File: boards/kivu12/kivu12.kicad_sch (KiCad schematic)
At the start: 26 parts, among them J1 P1, J10 SD, J11 GND, J12 LX2, J2 CIX, J3 BX, J4 LX1, J5 ANALOG, J6 POWER2, J7 BX, J9 POWER1

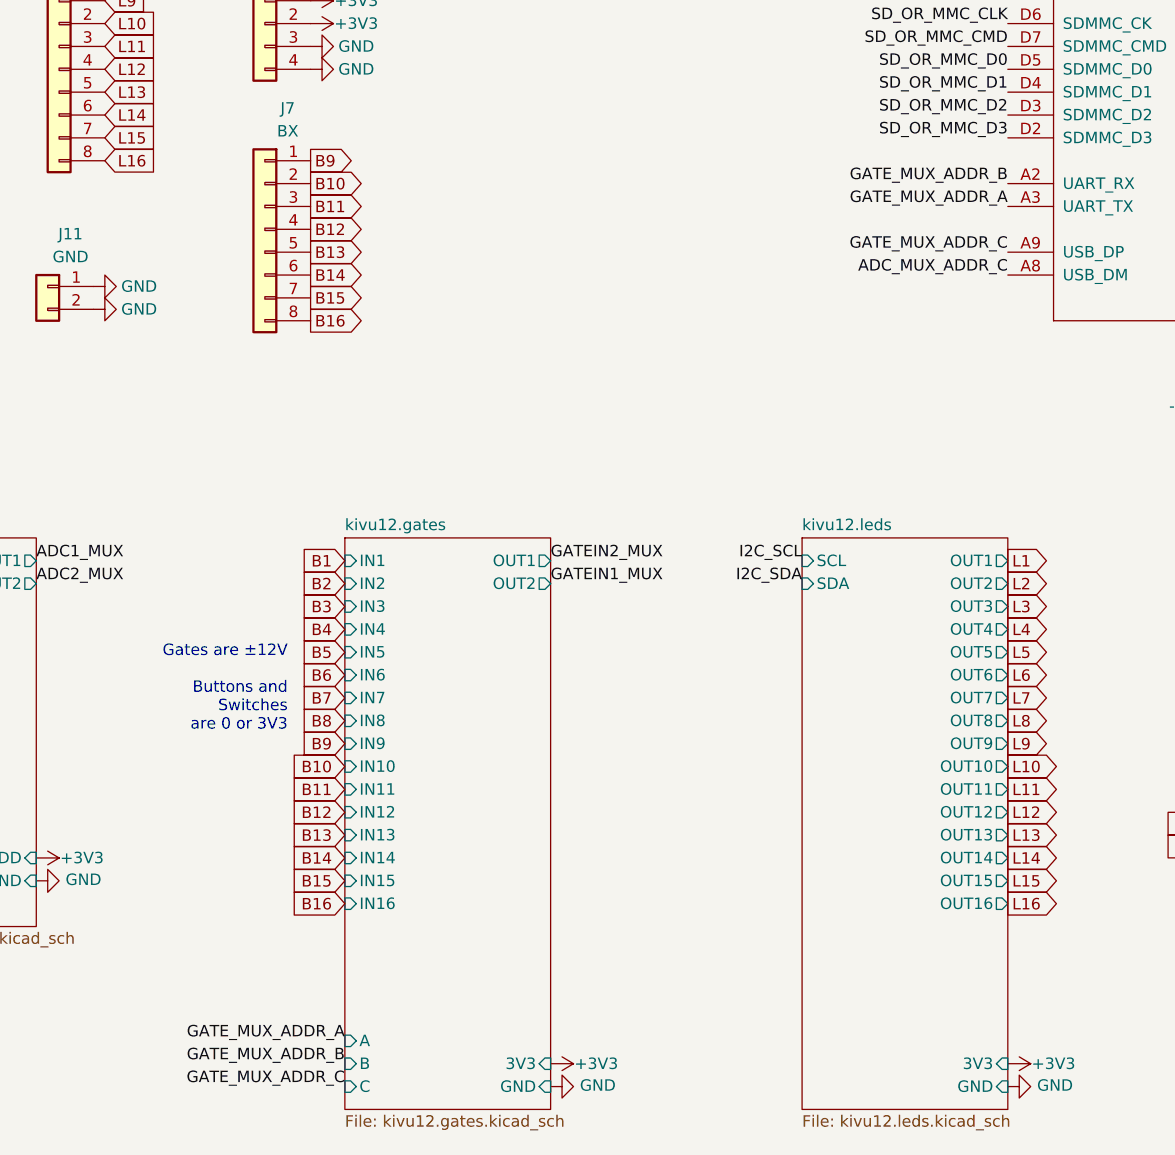
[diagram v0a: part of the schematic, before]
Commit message: Use shift register instead of multiplexer
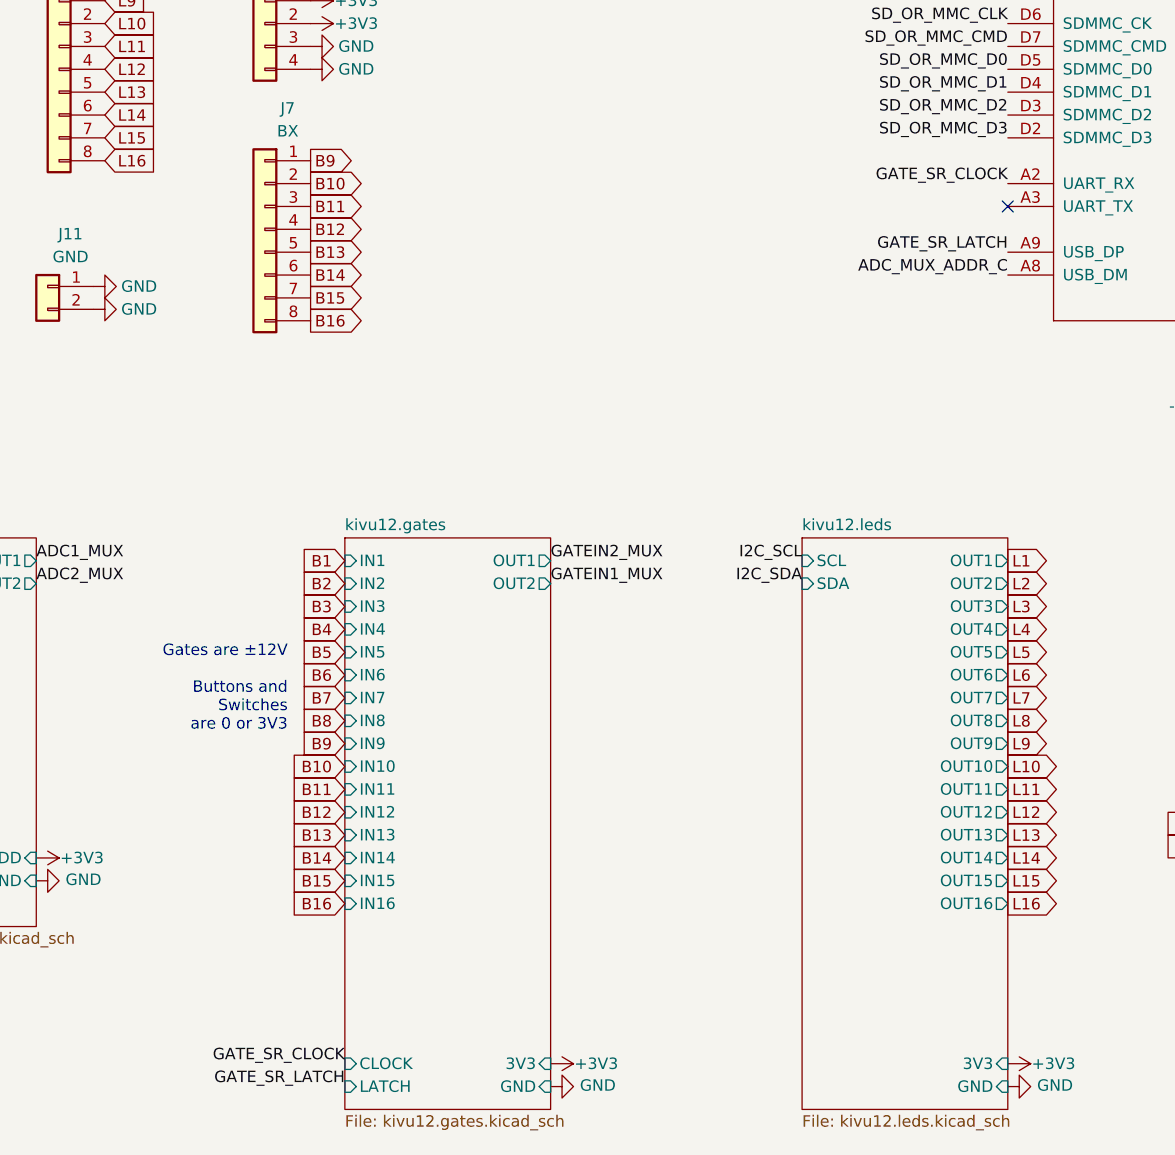
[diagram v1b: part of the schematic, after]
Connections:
- net GATE_MUX_ADDR_A: no longer names the net of DPSM1.A3 (UART_TX)
- net GATE_MUX_ADDR_B renamed GATE_SR_CLOCK
- net GATE_MUX_ADDR_C renamed GATE_SR_LATCH
- no-connect marks 1 -> 2
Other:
- sheet kivu12.gates ports: added CLOCK, LATCH; removed A, B, C
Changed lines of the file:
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@@
   (paper "A4")
   (no_connect (at 176.53 26.67))
+  (no_connect (at 158.75 77.47))
   (text "Just needed for BOM\nThey are:\n- 4x 2x5 female socket for the DPSM\n- 1x 1x36 Male header\n- 8x Jumpers"
     (at 246.38 57.15 0)
@@
     (effects (font (size 1.27 1.27)) (justify right bottom))
   )
-  (label "GATE_MUX_ADDR_C" (at 158.75 82.55 180)
+  (label "GATE_SR_LATCH" (at 158.75 82.55 180)
     (effects (font (size 1.27 1.27)) (justify right bottom))
   )
@@
     (effects (font (size 1.27 1.27)) (justify left bottom))
   )
-  (label "GATE_MUX_ADDR_B" (at 158.75 74.93 180)
+  (label "GATE_SR_CLOCK" (at 158.75 74.93 180)
     (effects (font (size 1.27 1.27)) (justify right bottom))
   )
@@
     (effects (font (size 1.27 1.27)) (justify right bottom))
   )
-  (label "GATE_MUX_ADDR_A" (at 158.75 77.47 180)
-    (effects (font (size 1.27 1.27)) (justify right bottom))
-  )
-  (label "GATE_MUX_ADDR_A" (at 85.09 170.18 180)
-    (effects (font (size 1.27 1.27)) (justify right bottom))
-  )
   (label "CV_OR_PITCH_ADSR2" (at 158.75 36.83 180)
     (effects (font (size 1.27 1.27)) (justify right bottom))
@@
     (effects (font (size 1.27 1.27)) (justify left bottom))
   )
-  (label "GATE_MUX_ADDR_C" (at 85.09 175.26 180)
+  (label "GATE_SR_LATCH" (at 85.09 175.26 180)
     (effects (font (size 1.27 1.27)) (justify right bottom))
   )
@@
     (effects (font (size 1.27 1.27)) (justify right bottom))
   )
-  (label "GATE_MUX_ADDR_B" (at 85.09 172.72 180)
+  (label "GATE_SR_CLOCK" (at 85.09 172.72 180)
     (effects (font (size 1.27 1.27)) (justify right bottom))
   )
@@
       (effects (font (size 1.27 1.27)) (justify left top))
     )
-    (pin "A" input (at 85.09 170.18 180)
-      (effects (font (size 1.27 1.27)) (justify left))
-    )
-    (pin "B" input (at 85.09 172.72 180)
-      (effects (font (size 1.27 1.27)) (justify left))
-    )
-    (pin "C" input (at 85.09 175.26 180)
-      (effects (font (size 1.27 1.27)) (justify left))
-    )
     (pin "GND" input (at 107.95 175.26 0)
       (effects (font (size 1.27 1.27)) (justify right))
@@
       (effects (font (size 1.27 1.27)) (justify right))
     )
+    (pin "CLOCK" input (at 85.09 172.72 180)
+      (effects (font (size 1.27 1.27)) (justify left))
+    )
+    (pin "LATCH" input (at 85.09 175.26 180)
+      (effects (font (size 1.27 1.27)) (justify left))
+    )
   )
   (sheet (at 237.49 114.3) (size 27.94 25.4) (fields_autoplaced)
@@
       (reference "L2") (unit 1) (value "Ferrite_Bead") (footprint "Inductor_SMD:L_0603_1608Metric")
     )
+    (path "/00000000-0000-0000-0000-000060958bfe/82553b7b-c84a-48f8-9d39-d10a95d00032"
+      (reference "R1") (unit 1) (value "1K") (footprint "Resistor_SMD:R_0603_1608Metric")
+    )
+    (path "/00000000-0000-0000-0000-000060958bfe/770ccc82-3d5c-4b0a-b0e0-ded04fb9c4a4"
+      (reference "R2") (unit 1) (value "1K") (footprint "Resistor_SMD:R_0603_1608Metric")
+    )
     (path "/00000000-0000-0000-0000-000060958bfe/00000000-0000-0000-0000-00006096181f"
       (reference "R4") (unit 1) (value "100k") (footprint "Resistor_SMD:R_0603_1608Metric")
@@
       (reference "R82") (unit 1) (value "100k") (footprint "Resistor_SMD:R_0603_1608Metric")
     )
+    (path "/00000000-0000-0000-0000-000060958bfe/f2085987-7c76-4ff8-9aa7-18ca1efdf565"
+      (reference "R84") (unit 1) (value "1M") (footprint "Resistor_SMD:R_0603_1608Metric")
+    )
+    (path "/00000000-0000-0000-0000-000060958bfe/2dc3d0d0-8b5b-411a-8647-713c967006df"
+      (reference "R85") (unit 1) (value "1M") (footprint "Resistor_SMD:R_0603_1608Metric")
+    )
+    (path "/00000000-0000-0000-0000-000060958bfe/0a6f3932-1e72-477c-8eac-9be588f1cdf1"
+      (reference "R86") (unit 1) (value "1M") (footprint "Resistor_SMD:R_0603_1608Metric")
+    )
+    (path "/00000000-0000-0000-0000-000060958bfe/ba210f35-64d9-449c-be38-94168bb82f72"
+      (reference "R87") (unit 1) (value "1M") (footprint "Resistor_SMD:R_0603_1608Metric")
+    )
+    (path "/00000000-0000-0000-0000-000060958bfe/81a97559-d3d4-449d-91ab-a57fa1158918"
+      (reference "R88") (unit 1) (value "1M") (footprint "Resistor_SMD:R_0603_1608Metric")
+    )
+    (path "/00000000-0000-0000-0000-000060958bfe/87f11fa2-ae56-4e61-92b9-2860c7aca4b9"
+      (reference "R89") (unit 1) (value "1M") (footprint "Resistor_SMD:R_0603_1608Metric")
+    )
+    (path "/00000000-0000-0000-0000-000060958bfe/94c3ef21-8293-4758-807d-a34c29effd8a"
+      (reference "R90") (unit 1) (value "1M") (footprint "Resistor_SMD:R_0603_1608Metric")
+    )
+    (path "/00000000-0000-0000-0000-000060958bfe/93f31d30-0541-43fa-894e-37559aa16097"
+      (reference "R91") (unit 1) (value "1M") (footprint "Resistor_SMD:R_0603_1608Metric")
+    )
+    (path "/00000000-0000-0000-0000-000060958bfe/babf4be3-e801-47cc-8080-d1264dca2374"
+      (reference "R92") (unit 1) (value "1M") (footprint "Resistor_SMD:R_0603_1608Metric")
+    )
+    (path "/00000000-0000-0000-0000-000060958bfe/57efddca-1d6b-4f5c-b73f-f5e525705528"
+      (reference "R93") (unit 1) (value "1M") (footprint "Resistor_SMD:R_0603_1608Metric")
+    )
+    (path "/00000000-0000-0000-0000-000060958bfe/f09979c3-8227-4499-8deb-e31f7b8bdb36"
+      (reference "R94") (unit 1) (value "1M") (footprint "Resistor_SMD:R_0603_1608Metric")
+    )
+    (path "/00000000-0000-0000-0000-000060958bfe/621ccc6c-066c-4e2b-a8a2-8903e37ef5fd"
+      (reference "R95") (unit 1) (value "1M") (footprint "Resistor_SMD:R_0603_1608Metric")
+    )
+    (path "/00000000-0000-0000-0000-000060958bfe/5d401222-6a33-4834-aab2-8277c7af83b1"
+      (reference "R96") (unit 1) (value "1M") (footprint "Resistor_SMD:R_0603_1608Metric")
+    )
+    (path "/00000000-0000-0000-0000-000060958bfe/6cf952f8-1fb1-4c7c-9e9c-f3f700a93d9f"
+      (reference "R97") (unit 1) (value "1M") (footprint "Resistor_SMD:R_0603_1608Metric")
+    )
+    (path "/00000000-0000-0000-0000-000060958bfe/7fbb2e29-07d0-4d24-81df-b9be5c060bff"
+      (reference "R98") (unit 1) (value "1M") (footprint "Resistor_SMD:R_0603_1608Metric")
+    )
+    (path "/00000000-0000-0000-0000-000060958bfe/72f453e7-c7d4-456e-b546-9e6a7b9b39e0"
+      (reference "R99") (unit 1) (value "1M") (footprint "Resistor_SMD:R_0603_1608Metric")
+    )
     (path "/00000000-0000-0000-0000-00006093b89c/00000000-0000-0000-0000-000060946352"
       (reference "U1") (unit 1) (value "4051") (footprint "Package_SO:TSSOP-16_4.4x5mm_P0.65mm")
@@
       (reference "U2") (unit 1) (value "4051") (footprint "Package_SO:TSSOP-16_4.4x5mm_P0.65mm")
     )
-    (path "/00000000-0000-0000-0000-000060958bfe/00000000-0000-0000-0000-00006095de74"
-      (reference "U3") (unit 1) (value "4051") (footprint "Package_SO:TSSOP-16_4.4x5mm_P0.65mm")
+    (path "/00000000-0000-0000-0000-000060958bfe/65257d55-0cd8-47f1-acfa-0975bb197ea3"
+      (reference "U3") (unit 1) (value "4021") (footprint "Package_SO:TSSOP-16_4.4x5mm_P0.65mm")
     )
-    (path "/00000000-0000-0000-0000-000060958bfe/00000000-0000-0000-0000-000060a214ca"
-      (reference "U4") (unit 1) (value "4051") (footprint "Package_SO:TSSOP-16_4.4x5mm_P0.65mm")
+    (path "/00000000-0000-0000-0000-000060958bfe/f6de3bd0-0d9e-409c-8b35-128e810a9e52"
+      (reference "U4") (unit 1) (value "4021") (footprint "Package_SO:TSSOP-16_4.4x5mm_P0.65mm")
     )
     (path "/00000000-0000-0000-0000-0000609afc8b/00000000-0000-0000-0000-000060ad63f1"
